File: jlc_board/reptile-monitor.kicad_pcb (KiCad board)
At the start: 4 copper layers, 38.1 x 38.1 mm, 30 parts, among them J1 AudioJack4_SwitchR1, J2 AudioJack4_SwitchR1, J3 PWR CONN, J4 UART, J5 I2C, J6 18-Lead FPC 0.5 mm - Vertical, SW1 RESET, U1 AP2112M-3.3, U2 TCA4307DGKR

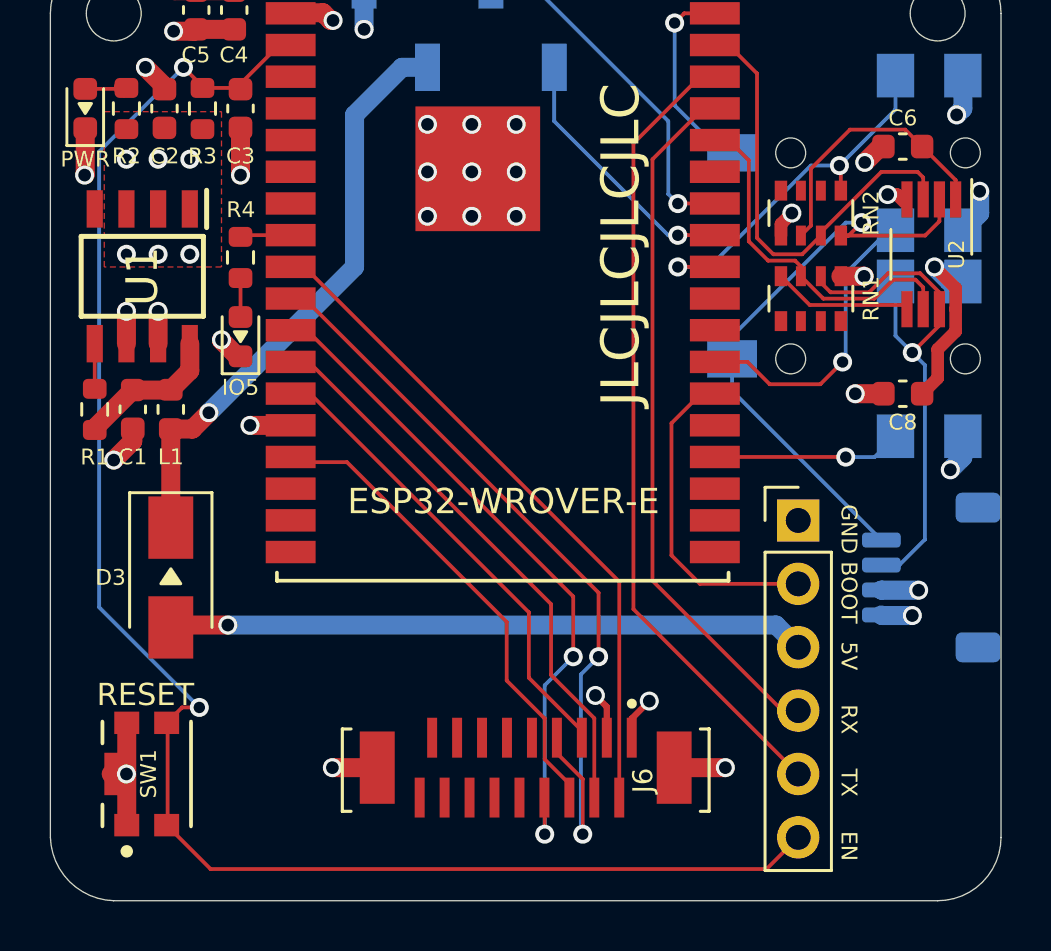
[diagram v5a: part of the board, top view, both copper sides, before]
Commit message: add raight angle tactile switch
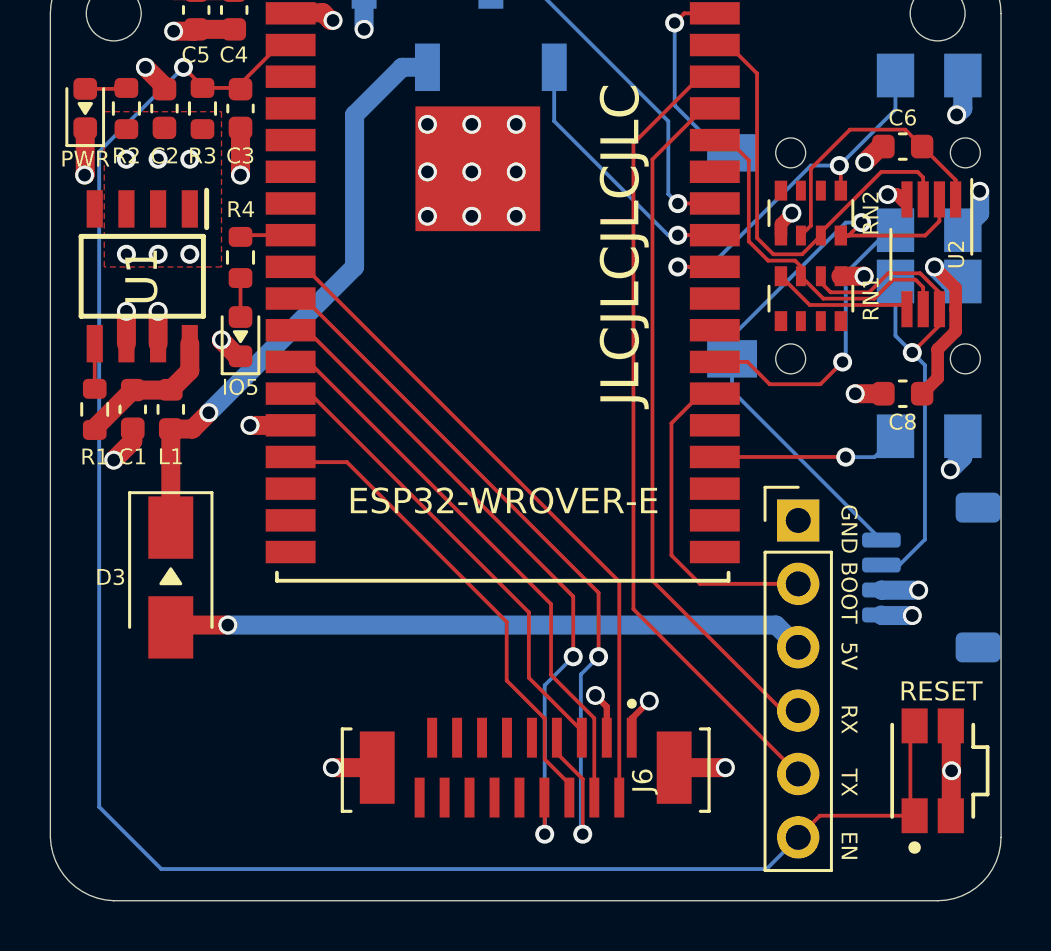
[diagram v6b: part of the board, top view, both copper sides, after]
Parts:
- SW1: footprint reptile-monitor:CK-KMR221GLFS-MFG -> reptile-monitor:Panasonic-EVQ-P7A01P-0-0-MFG
- moved SW1 31.8 mm to (151.8, 110.6)
- moved WAFFLE 1.82 mm to (132.5, 98.0)
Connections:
- SW1 pad 1: GND -> EN
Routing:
- net EN: track 67.0 -> 75.7 mm, vias 2 -> 1
- net GND: track 37.8 -> 37.2 mm

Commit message: updates
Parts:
- added D4: BAS316, reptile-monitor:D_SOD-323, F.Cu at (126.3, 110.7)
- added LS1: AST7525MATRQ, reptile-monitor:Mallory_Sonalert_Products_Inc-AST7525MATRQ-0-0-MFG, F.Cu at (121.2, 110.7)
- added Q1: 2SC1741, reptile-monitor:SOT-23, F.Cu at (121.6, 104.3)
- added R5: 1k, reptile-monitor:R_0603_1608Metric, F.Cu at (123.5, 100.5)
- D3: footprint reptile-monitor:D_SMA -> reptile-monitor:D_SOD-323
- moved D3 2.47 mm to (120.5, 100.5)
- moved J6 2.29 mm to (135.3, 112.8)
- moved U1 0.38 mm to (119.5, 90.8)
- moved C1 0.38 mm to (119.1, 96.1)
- moved L1 0.38 mm to (120.6, 96.1)
- moved R1 0.38 mm to (117.6, 96.1)
- moved D2 0.25 mm to (123.5, 93.2)
- moved R4 0.25 mm to (123.5, 90.0)
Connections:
- MD1 pad 8: (no net) -> /LED
- MD1 pad 9: /LED -> SPK
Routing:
- net SPK: track 0.00 -> 11.1 mm
- net Net-(D4-Pad2): track 0.00 -> 6.50 mm
- net IO26: track 31.5 -> 27.9 mm
- net Net-(D4-Pad1): track 0.00 -> 3.33 mm
- net Net-(Q1-Pad3): track 0.00 -> 2.96 mm
- net /5V_IN: track 25.6 -> 27.9 mm
- net SPI_SDO: track 19.5 -> 21.5 mm
- net IO25: track 27.0 -> 28.8 mm
- net IO27: track 27.2 -> 25.6 mm
- net +5V: track 23.7 -> 22.4 mm
- net SDA0: track 15.2 -> 13.9 mm
- net GND: track 37.2 -> 38.5 mm, vias 31 -> 32
- net RXD0: track 28.2 -> 27.1 mm
- net SPI_SCK: track 22.9 -> 23.9 mm
- net EN: track 75.7 -> 74.8 mm
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
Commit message: rev4.5
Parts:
- removed D3: Schottky, reptile-monitor:D_SOD-323
- removed J5: I2C, reptile-monitor:JST_SH_SM04B-SRSS-TB_1x04-1MP_P1.00mm_Horizontal
- added TP1: TestPoint_2Pole, Connector_PinHeader_2.54mm:PinHeader_1x02_P2.54mm_Vertical, F.Cu at (118.8, 103.8)
- D2: value IO5 -> 32
- Q1: footprint reptile-monitor:SOT-23 -> Package_TO_SOT_SMD:SOT-23
- RN1, RN2: footprint reptile-monitor:R_Array_Convex_4x0603 -> reptile-monitor:Panasonic-EXB-V8V103JV-0
- SW1: footprint reptile-monitor:Panasonic-EVQ-P7A01P-0-0-MFG -> reptile-monitor:AlpsAlpine_SKSCPD
- moved Q1 1.02 mm to (122.6, 104.3)
- moved SW1 0.76 mm to (152.6, 110.3)
- moved U2 0.54 mm to (151.1, 90.3)
- moved J1 0.51 mm to (154.3, 94.6)
- moved RN1 0.38 mm to (146.6, 92.1)
- moved C8 0.25 mm to (150.3, 95.2)
- moved D4 0.25 mm to (126.6, 110.7)
- moved C6 0.13 mm to (150.3, 85.7)
- moved RN2 0.13 mm to (146.6, 88.4), turned to -90 degrees
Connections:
- net /LED renamed IO32
- J4 pad 3: /5V_IN -> +5V
- RN1 pad 2: SDA_BUFFERED -> +3V3
- RN1 pad 3: SDA0 -> +3V3
- RN1 pad 4: /U2_RDY -> (no net)
- RN1 pad 6: (no net) -> /U2_RDY
- RN1 pad 7: (no net) -> SDA0
- RN1 pad 8: (no net) -> SDA_BUFFERED
- RN2 pad 2: /U2_EN -> +3V3
- RN2 pad 3: SCL0 -> +3V3
- RN2 pad 4: SCL_BUFFERED -> +3V3
- RN2 pad 5: IO5 -> SCL_BUFFERED
- RN2 pad 6: (no net) -> IO5
- RN2 pad 7: (no net) -> SCL0
- RN2 pad 8: (no net) -> /U2_EN
- U1 pad 2: (no net) -> +3V3
- U1 pad 3: (no net) -> +3V3
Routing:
- net +5V: track 22.4 -> 52.0 mm
- net /5V_IN: track 27.9 -> 0.00 mm, vias 1 -> 0
- net SDA_BUFFERED: track 21.4 -> 7.30 mm
- net SCL_BUFFERED: track 23.5 -> 11.9 mm
- net EN: track 74.8 -> 67.2 mm
- net /PWR_IN: track 5.92 -> 10.7 mm
- net SCL0: track 17.4 -> 13.2 mm
- net /U2_RDY: track 5.60 -> 2.87 mm
- net +3V3: track 18.8 -> 21.4 mm, vias 14 -> 13
- net /U2_EN: track 10.9 -> 8.50 mm
- net GND: track 38.5 -> 36.9 mm
- net IO5: track 15.2 -> 13.9 mm
- net Net-(D4-Pad2): track 6.50 -> 5.40 mm
- net SDA0: track 13.9 -> 15.0 mm
- net TXD0: track 31.8 -> 31.0 mm
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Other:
- board text added: "BT"
- board text added: "Rev. 4.5 Oct 2021"
- board text removed: "BOOT"
- board text removed: "Rev. 4 Aug 2021"
